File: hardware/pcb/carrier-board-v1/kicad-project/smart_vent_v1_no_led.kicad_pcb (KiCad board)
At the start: 2 copper layers, 45 x 34 mm, 16 parts, among them J1 PinHeader_1x02_P2.54mm_Vertic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, J2 PinHeader_1x03_P2.54mm_Vertic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, Q1 SOT-23, Q2 SOT-23, SW1 SW_DIP_SPSTx01_Slide_9.78x4.7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, U1 PinHeader_1x07_P2.54mm_Vertic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

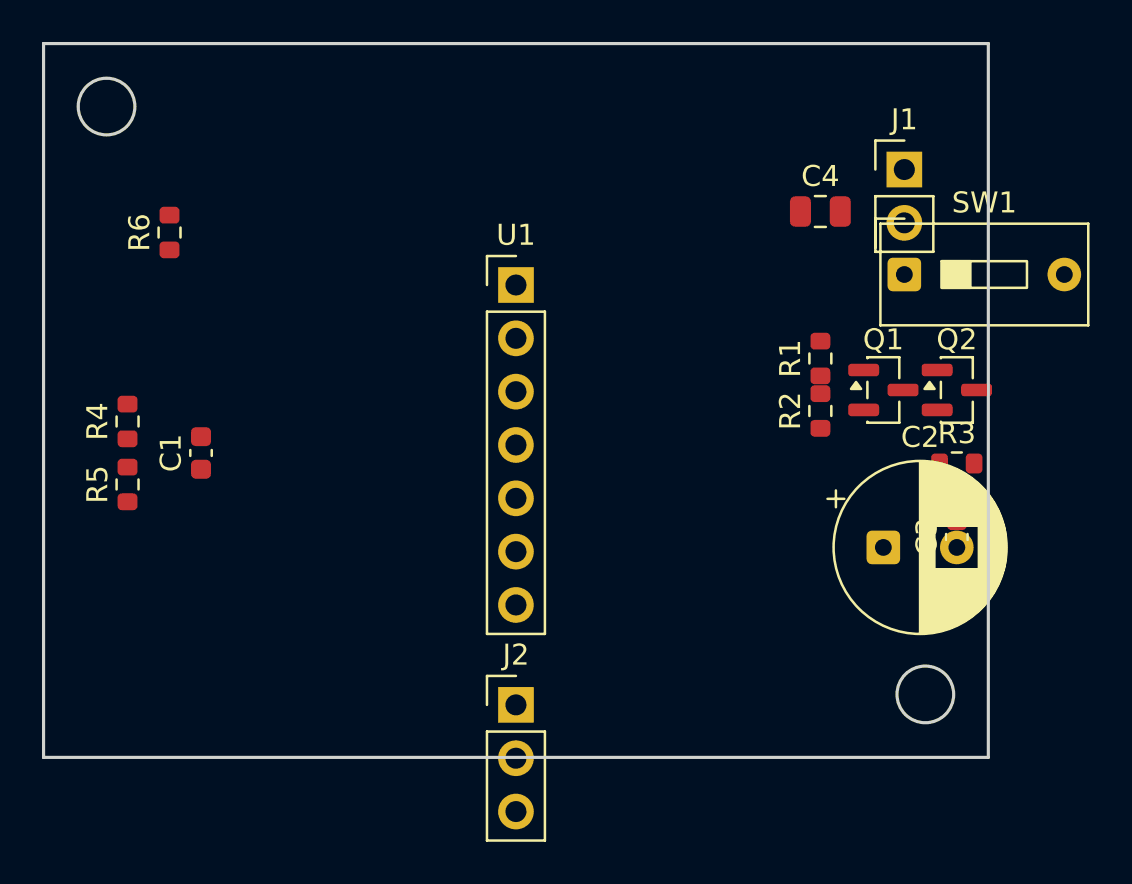
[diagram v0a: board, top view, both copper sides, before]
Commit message: Resolve all courtyard overlaps, shorts, and clearance violations in carrier board placement
DRC against real footprint sizes (issue #46) found the floorplan's
exact coordinates were sized around small SMD placeholders -- the
real stock substitutes for SW1 (THT slide switch, 10.37mm wide) and
C2 (THT radial cap, 8.59mm round) are much bigger, causing 3 shorts +
8 courtyard overlaps (with-LED) / 1 short + 5 overlaps (no-LED).

Adds nudge_apart.py, an iterative courtyard-separation solver, and
applies its resolved coordinates (plus one manual follow-up: J2's
last pad was landing past the board's bottom edge at its original
anchor, and separately collided with U1's placeholder footprint,
whose tall single-column shape doesn't represent the real XIAO
module) to build_board.py and place_smart_vent.py.

Re-running DRC on both variants: 0 shorts, 0 clearance violations,
0 courtyard overlaps, 0 board-edge clearance issues. Only cosmetic
silkscreen-text overlap remains. Regenerates the .kicad_pcb files
and the pipeline-validation Gerbers to match.
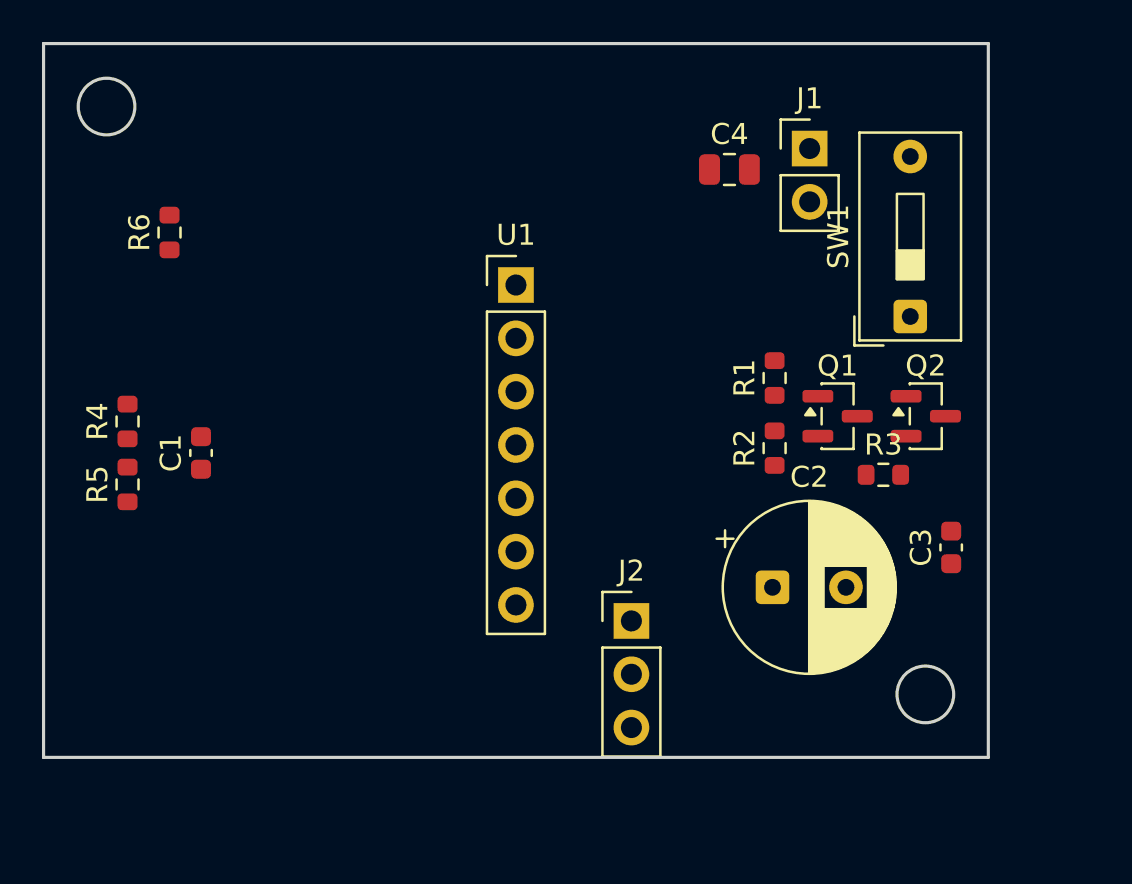
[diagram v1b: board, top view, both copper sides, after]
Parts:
- moved J2 6.80 mm to (58.0, 57.5)
- moved C2 5.61 mm to (64.7, 55.9)
- moved C4 4.77 mm to (62.7, 36.0)
- moved J1 4.62 mm to (66.5, 35.0)
- moved R3 3.54 mm to (70.0, 50.5)
- moved R2 2.81 mm to (64.8, 49.3)
- moved Q1 2.51 mm to (67.8, 47.8)
- moved R1 2.37 mm to (64.8, 45.9)
- moved SW1 2.02 mm to (71.3, 43.0), turned to 90 degrees
- moved Q2 1.94 mm to (72.0, 47.8)
- moved C3 0.57 mm to (73.2, 54.0)

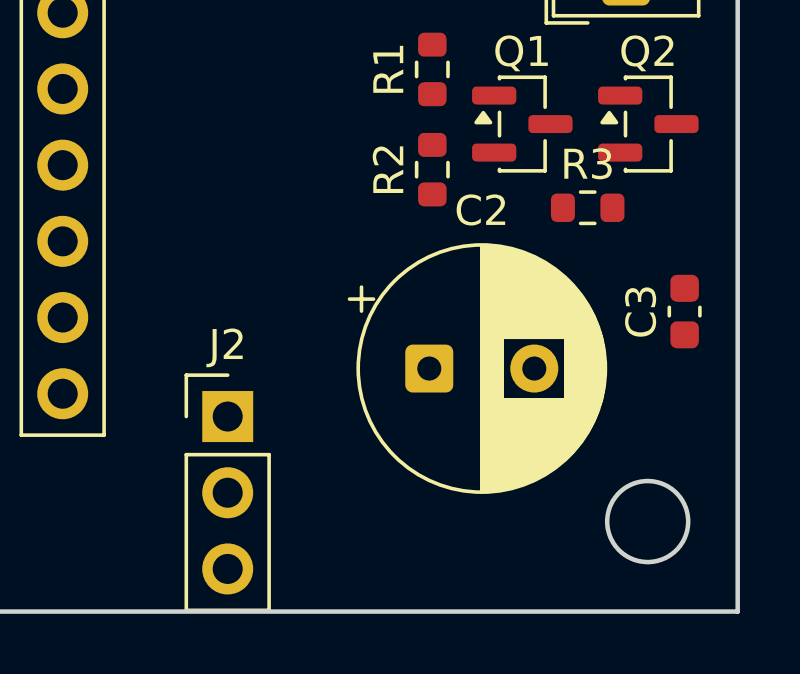
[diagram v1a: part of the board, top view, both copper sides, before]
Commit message: Resolve C2 footprint sourcing: Capacitor_SMD:CP_Elec_6.3x5.4 is in stock libs
The first placement pass searched only Capacitor_THT/Capacitor_Elec
libraries for C2's footprint and missed that the exact SMD part the
original netlist specified is filed under Capacitor_SMD.pretty. Swaps
it in for both variants in place of the bulkier THT radial stand-in,
narrowing issue #45 down to two remaining placeholders (U1, J1).

The real footprint's slightly different courtyard shape (9.69x7.19mm
vs the THT substitute's 8.59x8.59mm round) introduced one new minor
overlap with R2, fixed with a small nudge. DRC stays clean (0 shorts/
overlaps/clearance) on both variants after the fix.
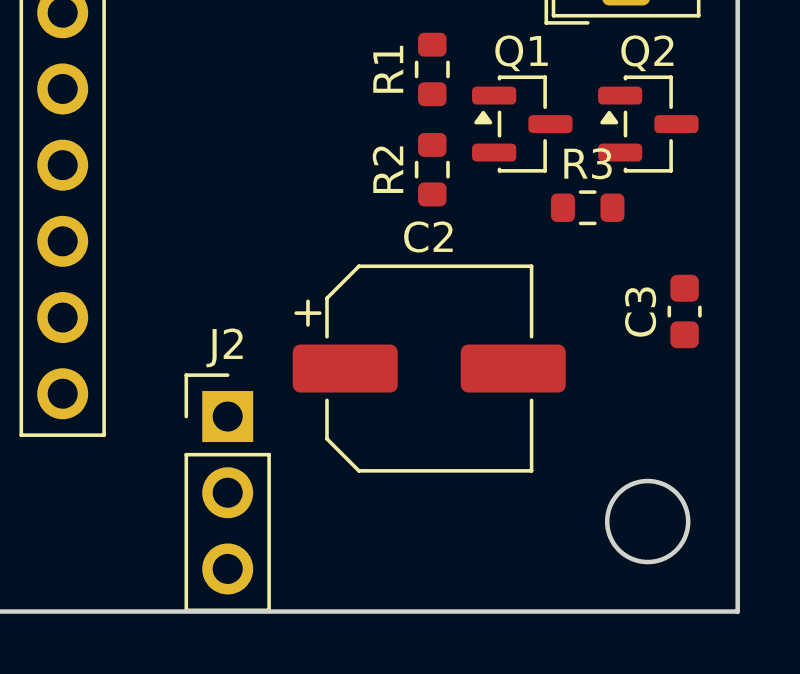
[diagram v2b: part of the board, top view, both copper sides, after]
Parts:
- C2: value CP_Radial_D8.0mm_P3.50mm -> CP_Elec_6.3x5.4; footprint CP_Radial_D8.0mm_P3.50mm -> CP_Elec_6.3x5.4
